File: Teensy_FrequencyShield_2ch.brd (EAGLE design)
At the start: 45.7 x 83.8 mm, 10 parts

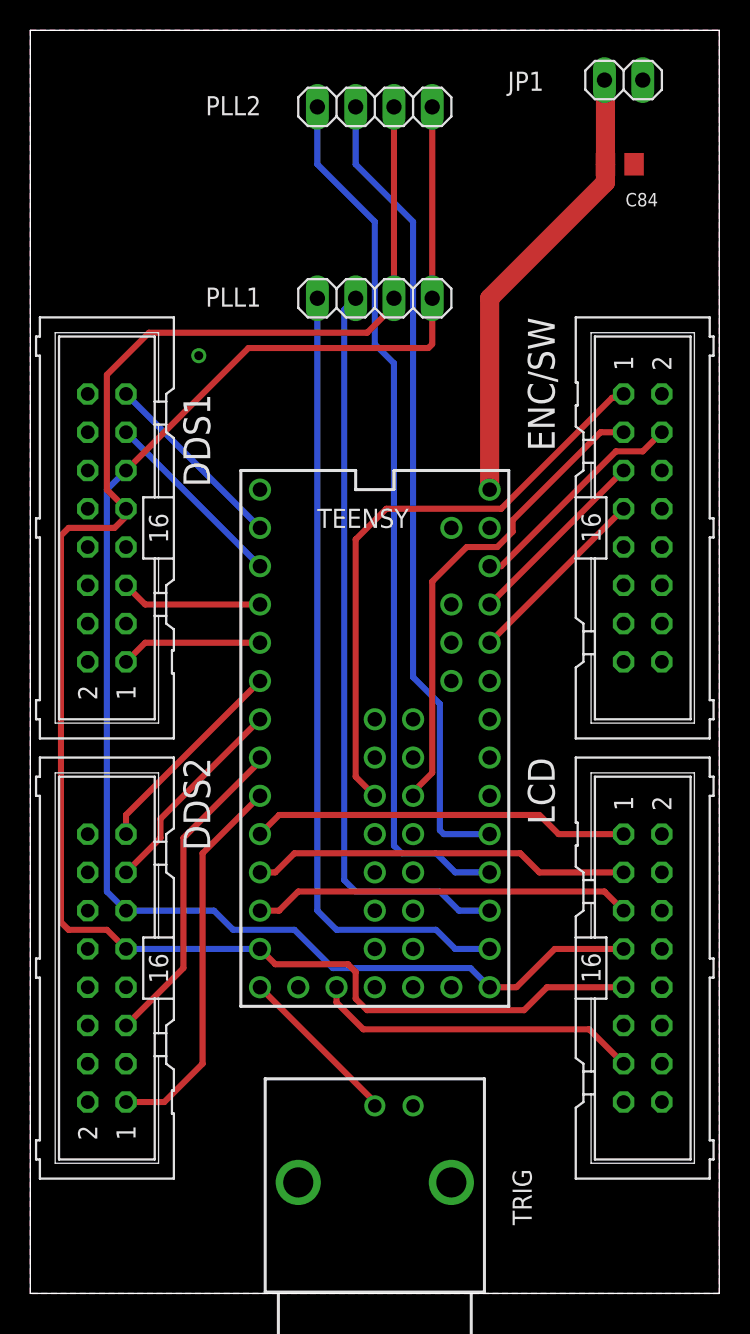
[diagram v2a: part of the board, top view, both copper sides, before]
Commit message: Re-routed Teensy_FreqShield to be a (mostly) 1-layer board
* Easier printing on LKPF machine
* GND connected through a few rivets to the top layer
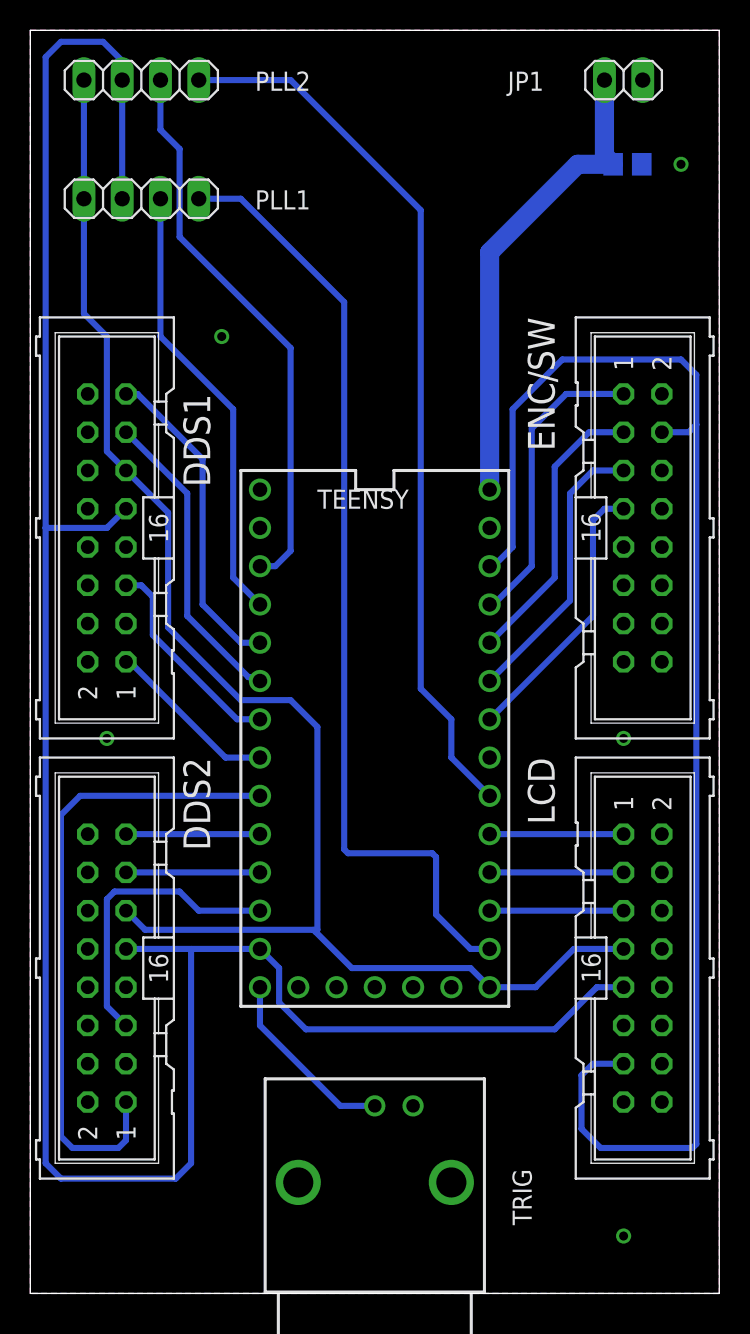
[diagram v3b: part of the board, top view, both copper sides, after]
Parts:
- TEENSY: value TEENSY_3.1_ALL_PINS_AND_PADS -> TEENSY_3.1_BASIC; device mcu-accessories:TEENSY_3.1_ALLPINS -> mcu-accessories:TEENSY_3.1_BASIC
- moved PLL1 16.8 mm to (-38.4, 42.2), turned to 0 degrees
- moved PLL2 15.6 mm to (-38.4, 50.0), turned to 0 degrees
- moved TEENSY 1.27 mm to (-22.9, 6.35)
- moved C84 0.51 mm to (-6.10, 44.5), flipped to the bottom, turned to 0 degrees
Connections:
- removed net AREF: TEENSY.AREF
- removed net DDS3_CS: TEENSY.26
- removed net DDS3_IOUPDATE: TEENSY.28
- removed net DDS3_PS0: TEENSY.27
- removed net DDS3_RESET: TEENSY.25
- removed net DDS4_IOUPDATE: TEENSY.21/A7
- removed net DDS4_PS0: TEENSY.20/A6
- removed net DDS4_RESET: TEENSY.18/A4
- removed net PLL3_LE: TEENSY.30
- removed net PLL3_MUX: TEENSY.29
- removed net PLL4_LE: TEENSY.32
- removed net PLL4_MUX: TEENSY.31
- removed net VUSB: TEENSY.VUSB
- net DDS1_CS: now also TEENSY.4; no longer TEENSY.1
- net DDS1_IOUPDATE: now also TEENSY.6; no longer TEENSY.3
- net DDS1_PS0: now also TEENSY.5; no longer TEENSY.2
- net DDS1_RESET: now also TEENSY.3; no longer TEENSY.0
- net DDS2_CS: now also TEENSY.9; no longer TEENSY.5
- net DDS2_PS0: now also TEENSY.10; no longer TEENSY.6
- net DDS2_RESET: now also TEENSY.8; no longer TEENSY.4
- net ENC_A: now also TEENSY.20/A6; no longer TEENSY.22/A8
- net ENC_B: now also TEENSY.21/A7; no longer TEENSY.23/A9
- net ENC_SW: now also TEENSY.23/A9; no longer TEENSY.24
- net GND: no longer TEENSY.GND2
- net LCD_CSB: now also TEENSY.15/A1; no longer TEENSY.10
- net LCD_RS: now also TEENSY.16/A2; no longer TEENSY.9
- net LCD_RST: now also TEENSY.17/A3; no longer TEENSY.8
- net PLL1_LE: now also TEENSY.2; no longer TEENSY.15/A1
- net PLL2_LE: now also TEENSY.1; no longer TEENSY.17/A3
- net PLL2_MUX: now also TEENSY.18/A4; no longer TEENSY.16/A2
- net SW1: now also TEENSY.22/A8; no longer TEENSY.33
- net VDD: no longer TEENSY.3.3V2
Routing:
- net VDD: track 36.9 -> 93.6 mm
- net MOSI: track 116.0 -> 156.9 mm
- net PLL1_LE: track 49.4 -> 29.7 mm
- net ENC_SW: track 39.3 -> 20.0 mm
- net DDS2_IOUPDATE: track 25.5 -> 42.5 mm
- net PLL2_LE: track 53.7 -> 37.3 mm
- net LCD_RS: track 25.2 -> 8.89 mm
- net LCD_RST: track 25.2 -> 8.89 mm
- net LCD_CSB: track 25.2 -> 8.89 mm
- net SW1: track 32.0 -> 19.0 mm
- net PLL1_MUX: track 53.1 -> 63.4 mm
- net DDS1_RESET: track 12.6 -> 21.4 mm
- net DDS1_CS: track 12.6 -> 20.5 mm
- net ENC_B: track 12.6 -> 18.8 mm
- net ENC_A: track 12.6 -> 18.4 mm
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
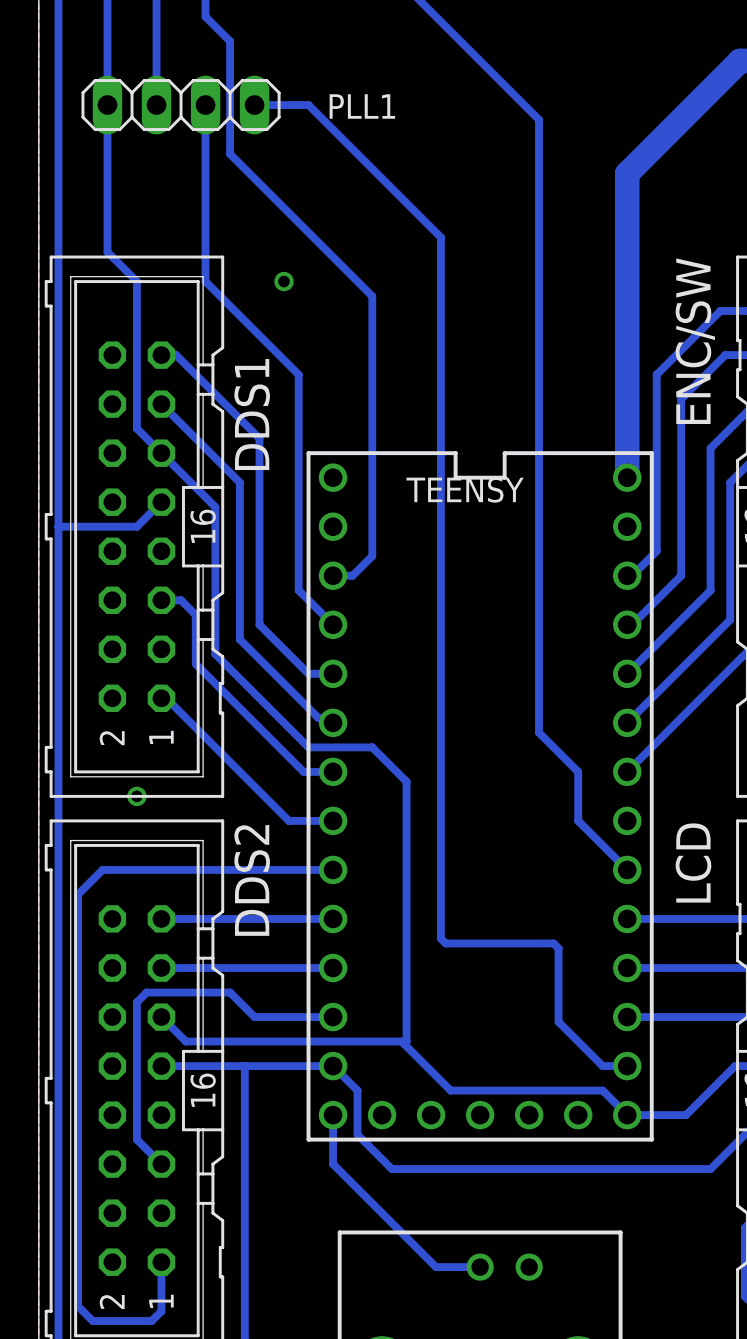
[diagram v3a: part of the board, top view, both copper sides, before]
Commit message: Re-routed several mcu-accessory boards to be (mostly) single-layer
Will make printing easier on LKPF machine.
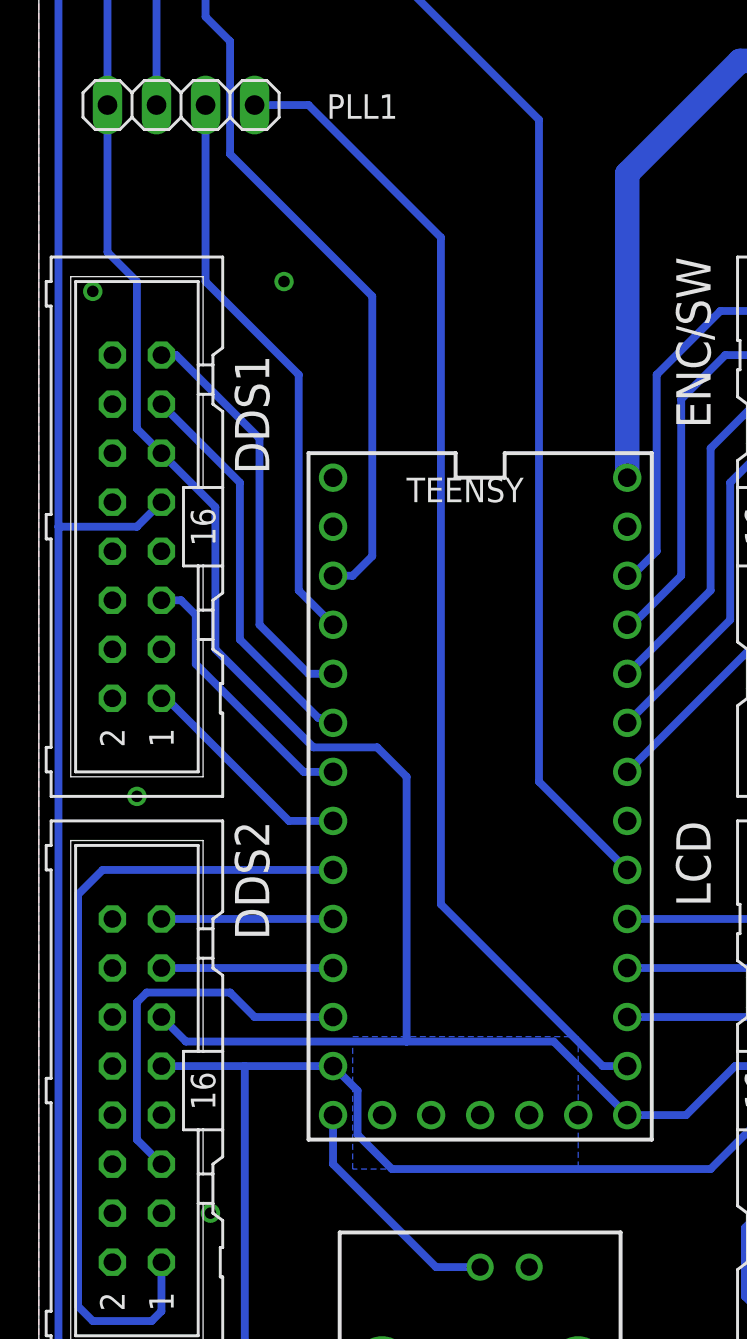
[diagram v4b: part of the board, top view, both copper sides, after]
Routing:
- net PLL1_MUX: track 63.4 -> 60.2 mm
- added copper zone on layer 16, net N$1
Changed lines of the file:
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@@
 <grid distance="0.01" unitdist="inch" unit="inch" style="lines" multiple="1" display="yes" altdistance="0.025" altunitdist="inch" altunit="inch"/>
 <layers>
-<layer number="1" name="Top" color="4" fill="1" visible="yes" active="yes"/>
+<layer number="1" name="Top" color="4" fill="1" visible="no" active="yes"/>
 <layer number="2" name="Route2" color="1" fill="3" visible="no" active="no"/>
 <layer number="3" name="Route3" color="4" fill="3" visible="no" active="no"/>
@@
 <contactref element="JP1" pad="2"/>
 <contactref element="TRIG" pad="2"/>
-<polygon width="0.4064" layer="16" isolate="0.762" thermals="no">
+<polygon width="0.4064" layer="16" isolate="0.762">
 <vertex x="-45.72" y="53.34"/>
 <vertex x="0" y="53.34"/>
@@
 <vertex x="-45.72" y="-30.48"/>
 </polygon>
+<via x="-36.83" y="-15.24" extent="1-16" drill="0.6" shape="square"/>
+<via x="-42.926" y="32.512" extent="1-16" drill="0.6" shape="square"/>
 </signal>
 <signal name="AGND">
@@
 <wire x1="-12.192" y1="-10.16" x2="-9.652" y2="-7.62" width="0.4064" layer="16"/>
 <wire x1="-9.652" y1="-7.62" x2="-6.35" y2="-7.62" width="0.4064" layer="16"/>
-<wire x1="-15.24" y1="-10.16" x2="-16.51" y2="-8.89" width="0.4064" layer="16"/>
-<wire x1="-16.51" y1="-8.89" x2="-24.384" y2="-8.89" width="0.4064" layer="16"/>
-<wire x1="-24.384" y1="-8.89" x2="-26.797" y2="-6.477" width="0.4064" layer="16"/>
-<wire x1="-26.797" y1="-6.477" x2="-26.924" y2="-6.35" width="0.4064" layer="16"/>
-<wire x1="-26.924" y1="-6.35" x2="-38.1" y2="-6.35" width="0.4064" layer="16"/>
 <wire x1="-38.1" y1="-6.35" x2="-39.37" y2="-5.08" width="0.4064" layer="16"/>
-<wire x1="-39.37" y1="24.13" x2="-36.576" y2="21.336" width="0.4064" layer="16"/>
-<wire x1="-36.576" y1="21.336" x2="-36.576" y2="13.716" width="0.4064" layer="16"/>
-<wire x1="-36.576" y1="13.716" x2="-31.75" y2="8.89" width="0.4064" layer="16"/>
-<wire x1="-31.75" y1="8.89" x2="-28.448" y2="8.89" width="0.4064" layer="16"/>
-<wire x1="-28.448" y1="8.89" x2="-26.67" y2="7.112" width="0.4064" layer="16"/>
-<wire x1="-26.67" y1="7.112" x2="-26.67" y2="-6.35" width="0.4064" layer="16"/>
-<wire x1="-26.67" y1="-6.35" x2="-26.797" y2="-6.477" width="0.4064" layer="16"/>
 <wire x1="-42.164" y1="50.038" x2="-42.164" y2="42.164" width="0.4064" layer="16"/>
 <wire x1="-39.37" y1="24.13" x2="-40.64" y2="25.4" width="0.4064" layer="16"/>
@@
 <wire x1="-40.64" y1="33.02" x2="-42.164" y2="34.544" width="0.4064" layer="16"/>
 <wire x1="-42.164" y1="34.544" x2="-42.164" y2="42.164" width="0.4064" layer="16"/>
+<wire x1="-38.1" y1="-6.35" x2="-26.67" y2="-6.35" width="0.4064" layer="16"/>
+<wire x1="-26.67" y1="-6.35" x2="-19.05" y2="-6.35" width="0.4064" layer="16"/>
+<wire x1="-19.05" y1="-6.35" x2="-15.24" y2="-10.16" width="0.4064" layer="16"/>
+<wire x1="-39.37" y1="24.13" x2="-36.576" y2="21.336" width="0.4064" layer="16"/>
+<wire x1="-36.576" y1="21.336" x2="-36.576" y2="13.97" width="0.4064" layer="16"/>
+<wire x1="-36.576" y1="13.97" x2="-31.496" y2="8.89" width="0.4064" layer="16"/>
+<wire x1="-31.496" y1="8.89" x2="-28.194" y2="8.89" width="0.4064" layer="16"/>
+<wire x1="-28.194" y1="8.89" x2="-26.67" y2="7.366" width="0.4064" layer="16"/>
+<wire x1="-26.67" y1="7.366" x2="-26.67" y2="-6.35" width="0.4064" layer="16"/>
 </signal>
 <signal name="PLL1_LE">
@@
 <contactref element="TEENSY" pad="14/A0"/>
 <wire x1="-31.75" y1="42.164" x2="-24.892" y2="35.306" width="0.4064" layer="16"/>
-<wire x1="-24.892" y1="35.306" x2="-24.892" y2="-1.016" width="0.4064" layer="16"/>
-<wire x1="-24.892" y1="-1.016" x2="-24.638" y2="-1.27" width="0.4064" layer="16"/>
-<wire x1="-24.638" y1="-1.27" x2="-19.05" y2="-1.27" width="0.4064" layer="16"/>
-<wire x1="-19.05" y1="-1.27" x2="-18.796" y2="-1.524" width="0.4064" layer="16"/>
-<wire x1="-18.796" y1="-1.524" x2="-18.796" y2="-5.334" width="0.4064" layer="16"/>
-<wire x1="-18.796" y1="-5.334" x2="-16.51" y2="-7.62" width="0.4064" layer="16"/>
-<wire x1="-16.51" y1="-7.62" x2="-15.24" y2="-7.62" width="0.4064" layer="16"/>
+<wire x1="-24.892" y1="35.306" x2="-24.892" y2="0.762" width="0.4064" layer="16"/>
 <wire x1="-31.75" y1="42.164" x2="-34.544" y2="42.164" width="0.4064" layer="16"/>
+<wire x1="-15.24" y1="-7.62" x2="-16.51" y2="-7.62" width="0.4064" layer="16"/>
+<wire x1="-16.51" y1="-7.62" x2="-24.892" y2="0.762" width="0.4064" layer="16"/>
 </signal>
 <signal name="PLL2_LE">
@@
 <contactref element="PLL2" pad="4"/>
 <contactref element="TEENSY" pad="18/A4"/>
-<wire x1="-15.24" y1="2.54" x2="-17.78" y2="5.08" width="0.4064" layer="16"/>
-<wire x1="-17.78" y1="5.08" x2="-17.78" y2="7.62" width="0.4064" layer="16"/>
-<wire x1="-17.78" y1="7.62" x2="-19.812" y2="9.652" width="0.4064" layer="16"/>
-<wire x1="-19.812" y1="9.652" x2="-19.812" y2="41.402" width="0.4064" layer="16"/>
+<wire x1="-19.812" y1="7.112" x2="-19.812" y2="41.402" width="0.4064" layer="16"/>
 <wire x1="-19.812" y1="41.402" x2="-28.448" y2="50.038" width="0.4064" layer="16"/>
 <wire x1="-28.448" y1="50.038" x2="-34.544" y2="50.038" width="0.4064" layer="16"/>
+<wire x1="-15.24" y1="2.54" x2="-19.812" y2="7.112" width="0.4064" layer="16"/>
 </signal>
 <signal name="DDS1_RESET">
@@
 <wire x1="-7.62" y1="45.024" x2="-7.046" y2="44.45" width="1.27" layer="16"/>
 </signal>
+<signal name="N$1">
+<polygon width="0.4064" layer="16" pour="cutout">
+<vertex x="-29.464" y="-6.096"/>
+<vertex x="-17.78" y="-6.096"/>
+<vertex x="-17.78" y="-12.954"/>
+<vertex x="-29.464" y="-12.954"/>
+</polygon>
+</signal>
 </signals>
